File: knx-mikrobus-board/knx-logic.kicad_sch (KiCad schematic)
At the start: 23 parts, among them U1 NCN5130, X1 16MHz

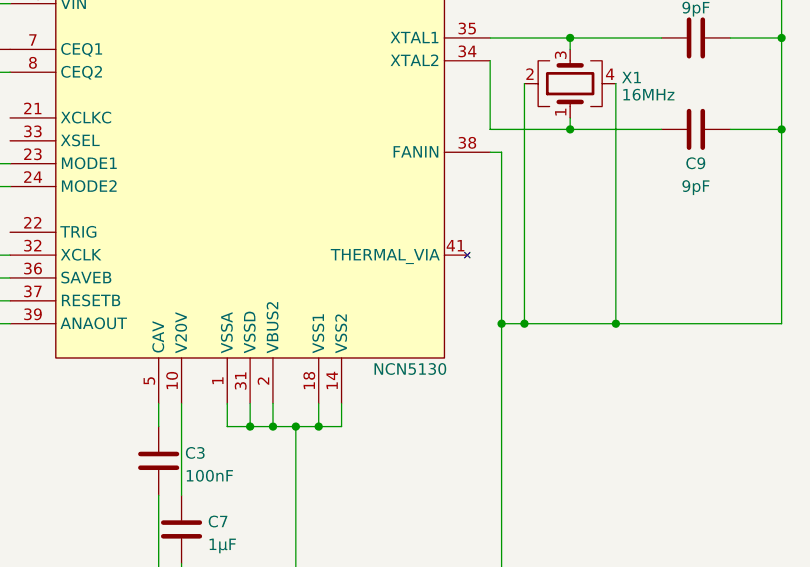
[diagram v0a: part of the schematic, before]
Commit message: knx: add ground plane
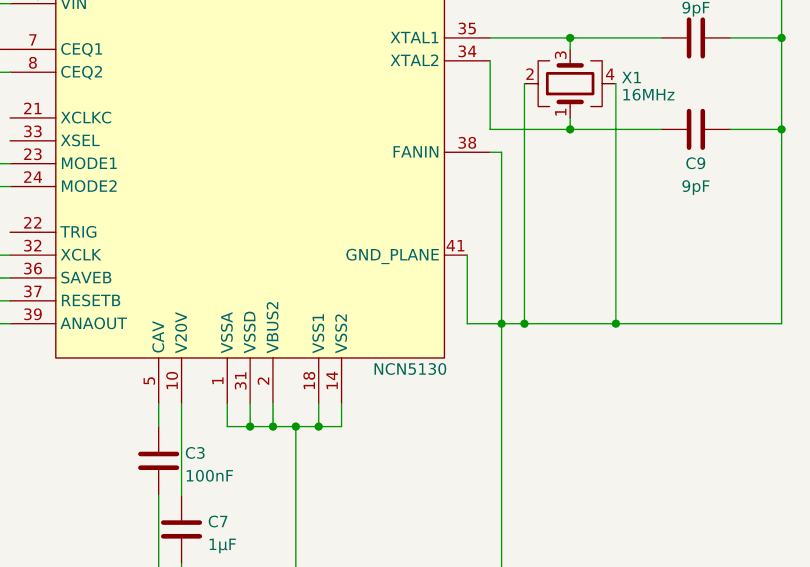
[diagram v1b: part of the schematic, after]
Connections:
- net GND: now also U1.41 (GND_PLANE)
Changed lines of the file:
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@@
+    (stroke (width 0) (type default) (color 0 0 0 0))
+  )
+  (wire (pts (xy 159.385 136.525) (xy 159.385 144.145))
     (stroke (width 0) (type default) (color 0 0 0 0))
   )
@@
     (stroke (width 0) (type default) (color 0 0 0 0))
   )
+  (wire (pts (xy 159.385 144.145) (xy 163.195 144.145))
+    (stroke (width 0) (type default) (color 0 0 0 0))
+  )
